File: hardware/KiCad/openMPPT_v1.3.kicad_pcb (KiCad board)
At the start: 2 copper layers, 137 parts, among them Q1 BSC030N08NS5, Q2 BSC030N08NS5, Q3 BSC030N08NS5, Q4 BSC030N08NS5, U1 STM32F072RBT6, U2 CC6937S8-3FB020, U3 CC6937S8-3FB020, U4 SCT2A25STER, U5 SY8120B1ABC

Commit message: layout progress
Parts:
- removed R15: 110kΩ, PCM_JLCPCB:R_0603
- moved C9 127.7 mm to (29.2, 142.0), turned to -90 degrees
- moved R3 126.6 mm to (30.5, 141.5), turned to -90 degrees
- moved R4 126.1 mm to (31.8, 141.5), turned to -90 degrees
- moved C20 124.9 mm to (78.1, 102.9)
- moved C21 124.9 mm to (78.1, 115.4)
- moved C22 124.9 mm to (78.4, 127.9)
- moved C23 124.9 mm to (78.4, 140.4)
- moved D1 121.2 mm to (26.4, 136.4), turned to -90 degrees
- moved UA1 119.5 mm to (31.1, 136.5), turned to 0 degrees
- moved C14 113.2 mm to (30.5, 132.0), turned to 0 degrees
- moved R8 108.1 mm to (183.5, 85.3), turned to -90 degrees
- moved L4 104.3 mm to (46.0, 124.5)
- moved C37 104.0 mm to (65.7, 112.5)
- moved C38 104.0 mm to (65.7, 110.5)
- moved C44 104.0 mm to (65.7, 100.5)
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
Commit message: rough layout ready, now just alignement todo
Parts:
- added H3: MountingHole, MountingHole:MountingHole_3.2mm_M3_DIN965, F.Cu at (158.0, 130.6)
- added H3: MountingHole, MountingHole:MountingHole_3.2mm_M3_DIN965, F.Cu at (128.5, 130.6)
- moved R9 110.6 mm to (130.9, 71.7), turned to 90 degrees
- moved R36 109.4 mm to (121.9, 71.7)
- moved C1 109.3 mm to (122.4, 58.1)
- moved C2 109.3 mm to (122.4, 50.1)
- moved C3 109.3 mm to (122.4, 52.1)
- moved C39 109.3 mm to (122.4, 48.1)
- moved C4 109.3 mm to (122.4, 54.1)
- moved C40 109.3 mm to (122.4, 66.1)
- moved C41 109.3 mm to (122.4, 64.1)
- moved C42 109.3 mm to (122.4, 62.1)
- moved C43 109.3 mm to (122.4, 60.1)
- moved C5 109.3 mm to (122.4, 56.1)
- moved D3 109.3 mm to (139.9, 80.3)
- moved L4 109.3 mm to (141.9, 72.3)
- moved Q2 109.3 mm to (135.4, 80.3)
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
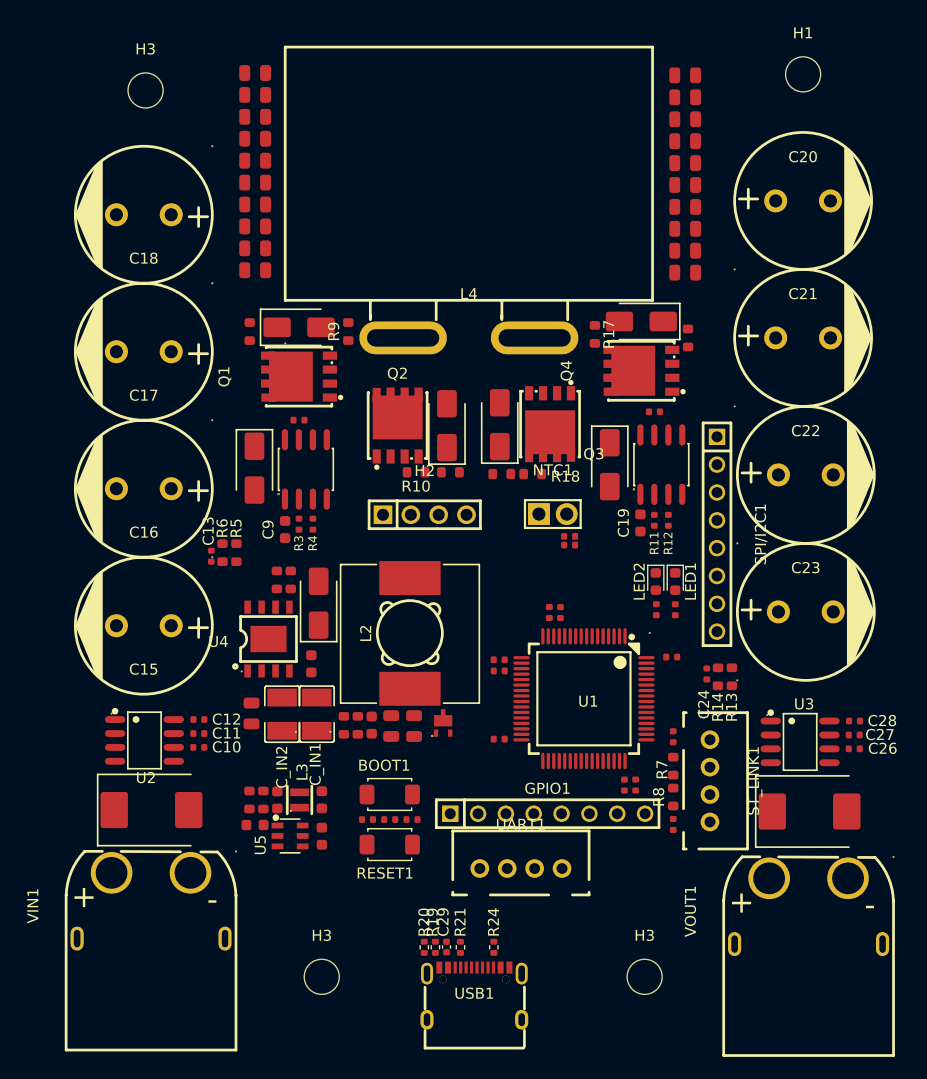
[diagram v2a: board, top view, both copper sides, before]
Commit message: added thermal "vias" directly to footprint
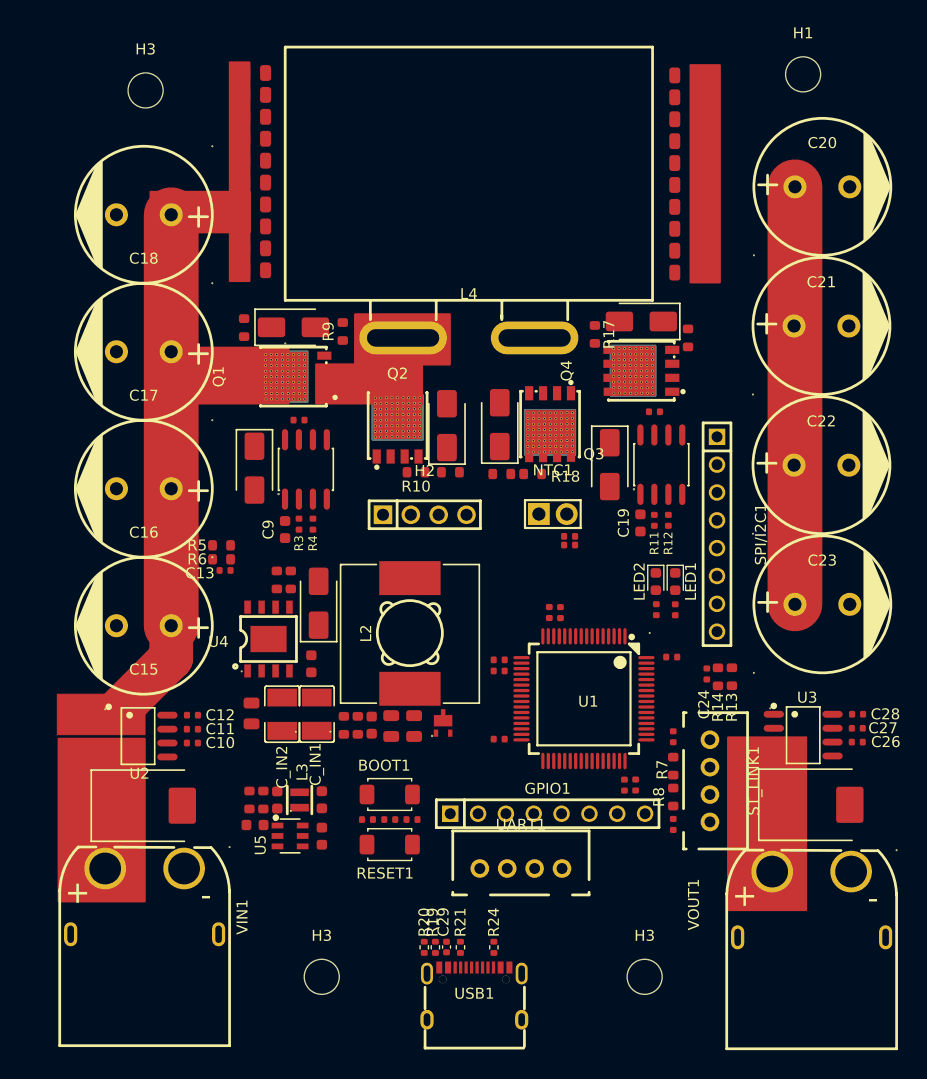
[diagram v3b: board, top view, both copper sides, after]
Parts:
- moved C20 2.18 mm to (174.2, 58.5)
- moved C21 2.00 mm to (174.1, 71.2)
- moved C13 1.80 mm to (119.7, 93.5), turned to 180 degrees
- moved C22 1.68 mm to (174.1, 83.9)
- moved C23 1.66 mm to (174.2, 96.6)
- moved R5 1.51 mm to (119.4, 91.2), turned to 0 degrees
- moved C10 0.71 mm to (116.7, 109.2)
- moved C11 0.71 mm to (116.7, 108.0)
- moved D10 0.71 mm to (112.4, 114.9)
- moved C12 0.71 mm to (116.7, 106.7)
- moved U2 0.71 mm to (111.8, 108.6)
- moved VIN1 0.71 mm to (112.4, 123.7)
- moved C26 0.68 mm to (177.4, 109.1)
- moved D11 0.68 mm to (173.3, 114.9)
- moved C27 0.68 mm to (177.4, 107.9)
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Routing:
- net IN_CAP: track 0.00 -> 47.2 mm
- net OUT_CAP: track 0.00 -> 38.1 mm
